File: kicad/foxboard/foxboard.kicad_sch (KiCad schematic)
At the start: 183 parts, among them J2 USB_C_Receptacle_USB2.0, K1 KEYSW, K10 KEYSW, K11 KEYSW, K12 KEYSW, K13 KEYSW, K14 KEYSW, K15 KEYSW, K16 KEYSW, K17 KEYSW, K18 KEYSW, K19 KEYSW, K2 KEYSW, K20 KEYSW, K21 KEYSW, K22 KEYSW, K23 KEYSW, K24 KEYSW, K25 KEYSW, K26 KEYSW, K27 KEYSW, K28 KEYSW, K29 KEYSW, K3 KEYSW, K30 KEYSW, K31 KEYSW, K32 KEYSW, K33 KEYSW, K34 KEYSW, K35 KEYSW, K36 KEYSW, K37 KEYSW, K38 KEYSW, K39 KEYSW, K4 KEYSW, K40 KEYSW, K41 KEYSW, K42 KEYSW, K43 KEYSW, K44 KEYSW, K45 KEYSW, K46 KEYSW, K47 KEYSW, K48 KEYSW, K49 KEYSW, K5 KEYSW, K50 KEYSW, K51 KEYSW, K52 KEYSW, K53 KEYSW, K54 KEYSW, K55 KEYSW, K56 KEYSW, K57 KEYSW, K58 KEYSW, K59 KEYSW, K6 KEYSW, K60 KEYSW, K61 KEYSW, K62 KEYSW, K63 KEYSW, K64 KEYSW, K65 KEYSW, K66 KEYSW, K67 KEYSW, K68 KEYSW, K69 KEYSW, K7 KEYSW, K70 KEYSW, K71 KEYSW, K72 KEYSW, K73 KEYSW, K74 KEYSW, K75 KEYSW, K76 KEYSW, K77 KEYSW, K78 KEYSW, K79 KEYSW, K8 KEYSW, K80 KEYSW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

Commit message: make sure all connections are connected, change resistor package to 0805
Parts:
- D52: MPN C2875153 -> C24372
- R5, R6: footprint custom:RESC1608X55N -> Resistor_SMD:R_0805_2012Metric
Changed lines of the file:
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@@
 			)
 		)
-		(property "Footprint" "custom:RESC1608X55N"
+		(property "Footprint" "Resistor_SMD:R_0805_2012Metric"
 			(at 254 160.528 90)
 			(effects
@@
 			)
 		)
-		(property "MPN" "C2875153"
+		(property "MPN" "C24372"
 			(at 45.72 86.36 90)
 			(effects
@@
 			)
 		)
-		(property "Footprint" "custom:RESC1608X55N"
+		(property "Footprint" "Resistor_SMD:R_0805_2012Metric"
 			(at 254 157.988 90)
 			(effects

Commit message: fix
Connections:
- net row 5: now also U2.5 (3_LRCLK2); no longer U2.2 (0_RX1_CRX2_CS1)
- net row 6: now also U2.6 (4_BCLK2); no longer U2.1 (GND)

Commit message: wip v2
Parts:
- removed U2: Teensy4.1, teensy:Teensy41, symbol teensy:Teensy4.1
- added C1, C2: 10u, symbol Device:C
- added C10, C11, C12, C13, C5, C6, C7, C8, C9: 100n, symbol Device:C
- added C14, C3: 1u, symbol Device:C
- added C15, C4: C, symbol Device:C
- added C16, C17: 15p, symbol Device:C
- added J1: Conn_01x02, symbol Connector_Generic:Conn_01x02
- added R1, R2: 27.4, symbol Device:R
- added R3: 1k, symbol Device:R
- added R4: DNF, symbol Device:R
- added U1: RP2040, RP2040_minimal:RP2040-QFN-56, symbol MCU_RaspberryPi_RP2040:RP2040
- added U2: NCP1117-3.3_SOT223, Package_TO_SOT_SMD:SOT-223-3_TabPin2, symbol Regulator_Linear:NCP1117-3.3_SOT223
- added U3: W25Q128JVS, Package_SO:SOIC-8_5.3x5.3mm_P1.27mm, symbol Memory_Flash:W25Q128JVS
- added Y1: ABM8-272-T3, symbol Device:Crystal_GND24
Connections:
- net GND: now also C1.2, C10.2, C11.2, C12.2, C13.2, C14.2, C15.2, C16.1, C17.1, C2.1, C3.2, C4.2, C5.2, C6.2, C7.2, C8.2, C9.2, J1.1 (Pin_1), U2.1 (GND), U3.4 (GND), Y1.2 (G), Y1.4 (G)
- net VBUS: now also C1.1, U2.3 (VI)
- net col 1: now also U1.8 (GPIO6)
- net col 10: now also U1.18 (GPIO15)
- net col 11: now also U1.27 (GPIO16)
- net col 12: now also U1.28 (GPIO17)
- net col 13: now also U1.29 (GPIO18)
- net col 14: now also U1.30 (GPIO19)
- net col 15: now also U1.31 (GPIO20)
- net col 16: now also U1.32 (GPIO21)
- net col 17: now also U1.34 (GPIO22)
- net col 2: now also U1.9 (GPIO7)
- net col 3: now also U1.11 (GPIO8)
- net col 4: now also U1.12 (GPIO9)
- net col 5: now also U1.13 (GPIO10)
- net col 6: now also U1.14 (GPIO11)
- net col 7: now also U1.15 (GPIO12)
- net col 8: now also U1.16 (GPIO13)
- net col 9: now also U1.17 (GPIO14)
- net row 1: now also U1.2 (GPIO0)
- net row 2: now also U1.3 (GPIO1)
- net row 3: now also U1.4 (GPIO2)
- net row 4: now also U1.5 (GPIO3)
- net row 5: now also U1.6 (GPIO4)
- net row 6: now also U1.7 (GPIO5)
- net USB_D-: now reaches J2.A7 (D-), J2.B7 (D-)
- net USB_D-: now also R1.2
- net USB_D+: now reaches J2.A6 (D+), J2.B6 (D+)
- net USB_D+: now also R2.1
- new net: R3.1, R4.2, U3.1 (~{CS})
- new net: J1.2 (Pin_2), R3.2
- new net: R2.2, U1.46 (USB_DM)
- new net: R1.1, U1.47 (USB_DP)
- new net +1.1V: C3.1, C4.1, C5.1, U1.23 (DVDD), U1.45 (VREG_VOUT), U1.50 (DVDD)
- new net +3.3V: C10.1, C11.1, C12.1, C13.1, C14.1, C15.1, C2.2, C6.1, C7.1, C8.1, C9.1, R4.1, U1.1 (IOVDD), U1.10 (IOVDD), U1.22 (IOVDD), U1.33 (IOVDD), U1.42 (IOVDD), U1.43 (ADC_AVDD), U1.44 (VREG_IN), U1.48 (USB_VDD), U1.49 (IOVDD), U2.2 (VO), U3.8 (VCC)
- new net XIN: C17.2, U1.20 (XIN), Y1.1
- new net XOUT: C16.2, U1.21 (XOUT), Y1.3
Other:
- moved on the sheet: J2, R5, R6

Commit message: fix most violations
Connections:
- net GND: now also U1.19 (TESTEN), U1.57 (GND)
- net QSPI_SS: now reaches R3.1, R4.2, U3.1 (~{CS})
- net QSPI_SS: now also U1.56 (QSPI_SS)
- net QSPI_SD3: now reaches U1.51 (QSPI_SD3)
- net QSPI_SD3: now also U3.7 (~{HOLD}/~{RESET}/IO_{3})
- net QSPI_SCLK: now reaches U1.52 (QSPI_SCLK)
- net QSPI_SCLK: now also U3.6 (CLK)
- net QSPI_SDO: now reaches U1.53 (QSPI_SD0)
- net QSPI_SDO: now also U3.5 (DI/IO_{0})
- net QSPI_SD2: now reaches U1.54 (QSPI_SD2)
- net QSPI_SD2: now also U3.3 (~{WP}/IO_{2})
- net QSPI_SD1: now reaches U1.55 (QSPI_SD1)
- net QSPI_SD1: now also U3.2 (DO/IO_{1})
- no-connect marks 2 -> 12
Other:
- moved on the sheet: J1, R3

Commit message: add powerflags
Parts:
- D56:  MPN C24372 -> (none); MPN (none) -> C24372
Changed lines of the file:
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@@
 	)
 	(junction
-		(at 55.88 236.22)
-		(diameter 0)
-		(color 0 0 0 0)
-	)
-	(junction
 		(at 317.5 49.53)
 		(diameter 0)
@@
 	)
 	(junction
+		(at 347.98 161.29)
+		(diameter 0)
+		(color 0 0 0 0)
+	)
+	(junction
 		(at 250.19 90.17)
 		(diameter 0)
@@
 	)
 	(junction
+		(at 55.88 236.22)
+		(diameter 0)
+		(color 0 0 0 0)
+	)
+	(junction
 		(at 238.76 124.46)
 		(diameter 0)
@@
 	)
 	(junction
+		(at 165.1 284.48)
+		(diameter 0)
+		(color 0 0 0 0)
+	)
+	(junction
 		(at 231.14 73.66)
 		(diameter 0)
@@
 	(wire
 		(pts
+			(xy 55.88 236.22) (xy 71.12 236.22)
+		)
+		(stroke
+			(width 0)
+			(type default)
+		)
+	)
+	(wire
+		(pts
 			(xy 60.96 82.55) (xy 60.96 100.33)
 		)
@@
 	(wire
 		(pts
+			(xy 165.1 284.48) (xy 172.72 284.48)
+		)
+		(stroke
+			(width 0)
+			(type default)
+		)
+	)
+	(wire
+		(pts
 			(xy 128.27 139.7) (xy 135.89 139.7)
 		)
@@
 	(wire
 		(pts
-			(xy 55.88 236.22) (xy 69.85 236.22)
-		)
-		(stroke
-			(width 0)
-			(type default)
-		)
-	)
-	(wire
-		(pts
 			(xy 165.1 39.37) (xy 165.1 49.53)
 		)
@@
 		)
 	)
-	(label ""
-		(at 55.88 236.22 0)
-		(effects
-			(font
-				(size 1.27 1.27)
-			)
-			(justify left bottom)
-		)
-	)
 	(label "QSPI_SS"
 		(at 133.35 201.93 180)
@@
 	(global_label "XIN"
 		(shape input)
-		(at 69.85 236.22 0)
+		(at 71.12 236.22 0)
 		(fields_autoplaced yes)
 		(effects
@@
 		)
 		(property "Intersheetrefs" "${INTERSHEET_REFS}"
-			(at 75.98 236.22 0)
+			(at 77.25 236.22 0)
 			(hide yes)
 			(show_name no)
@@
 	)
 	(symbol
+		(lib_id "power:PWR_FLAG")
+		(at 172.72 284.48 0)
+		(unit 1)
+		(body_style 1)
+		(exclude_from_sim no)
+		(in_bom yes)
+		(on_board yes)
+		(in_pos_files yes)
+		(dnp no)
+		(fields_autoplaced yes)
+		(property "Reference" "#FLG01"
+			(at 172.72 282.575 0)
+			(hide yes)
+			(show_name no)
+			(do_not_autoplace no)
+			(effects
+				(font
+					(size 1.27 1.27)
+				)
+			)
+		)
+		(property "Value" "PWR_FLAG"
+			(at 172.72 279.4 0)
+			(show_name no)
+			(do_not_autoplace no)
+			(effects
+				(font
+					(size 1.27 1.27)
+				)
+			)
+		)
+		(property "Footprint" ""
+			(at 172.72 284.48 0)
+			(hide yes)
+			(show_name no)
+			(do_not_autoplace no)
+			(effects
+				(font
+					(size 1.27 1.27)
+				)
+			)
+		)
+		(property "Datasheet" ""
+			(at 172.72 284.48 0)
+			(hide yes)
+			(show_name no)
+			(do_not_autoplace no)
+			(effects
+				(font
+					(size 1.27 1.27)
+				)
+			)
+		)
+		(property "Description" "Special symbol for telling ERC where power comes from"
+			(at 172.72 284.48 0)
+			(hide yes)
+			(show_name no)
+			(do_not_autoplace no)
+			(effects
+				(font
+					(size 1.27 1.27)
+				)
+			)
+		)
+		(pin "1"
+		)
+		(instances
+			(project "foxboard"
+				(path "/06390bb7-84c9-4afb-a691-da3db02fcaf4"
+					(reference "#FLG01")
+					(unit 1)
+				)
+			)
+		)
+	)
+	(symbol
 		(lib_id "Device:D")
 		(at 26.67 120.65 90)
@@
 		(in_pos_files yes)
 		(dnp no)
-		(fields_autoplaced yes)
 		(property "Reference" "#PWR06"
 			(at 345.44 163.83 0)
@@
 		)
 		(property "Value" "VBUS"
-			(at 345.44 154.94 0)
+			(at 345.44 155.702 0)
 			(show_name no)
 			(do_not_autoplace no)
@@
 			)
 		)
-		(property " MPN" "C24372"
+		(property "MPN" "C24372"
 			(at 129.54 86.36 90)
 			(hide yes)
@@
 					(unit 1)
 				)
+			)
+		)
+	)
+	(symbol
+		(lib_id "power:PWR_FLAG")
+		(at 347.98 161.29 0)
+		(unit 1)
+		(body_style 1)
+		(exclude_from_sim no)
+		(in_bom yes)
+		(on_board yes)
+		(in_pos_files yes)
+		(dnp no)
+		(fields_autoplaced yes)
+		(property "Reference" "#FLG02"
+			(at 347.98 159.385 0)
+			(hide yes)
+			(show_name no)
+			(do_not_autoplace no)
+			(effects
+				(font
+					(size 1.27 1.27)
+				)
+			)
+		)
+		(property "Value" "PWR_FLAG"
+			(at 347.98 156.21 0)
+			(show_name no)
+			(do_not_autoplace no)
+			(effects
+				(font
+					(size 1.27 1.27)
+				)
+			)
+		)
+		(property "Footprint" ""
+			(at 347.98 161.29 0)
+			(hide yes)
+			(show_name no)
+			(do_not_autoplace no)
+			(effects
+				(font
+					(size 1.27 1.27)
+				)
+			)
+		)
+		(property "Datasheet" ""
+			(at 347.98 161.29 0)
+			(hide yes)
+			(show_name no)
+			(do_not_autoplace no)
+			(effects
+				(font
+					(size 1.27 1.27)
+				)
+			)
+		)
+		(property "Description" "Special symbol for telling ERC where power comes from"
+			(at 347.98 161.29 0)
+			(hide yes)
+			(show_name no)
+			(do_not_autoplace no)
+			(effects
+				(font
+					(size 1.27 1.27)
+				)
+			)
+		)
+		(pin "1"
+		)
+		(instances
+			(project "foxboard"
+				(path "/06390bb7-84c9-4afb-a691-da3db02fcaf4"
+					(reference "#FLG02")
+					(unit 1)
+				)

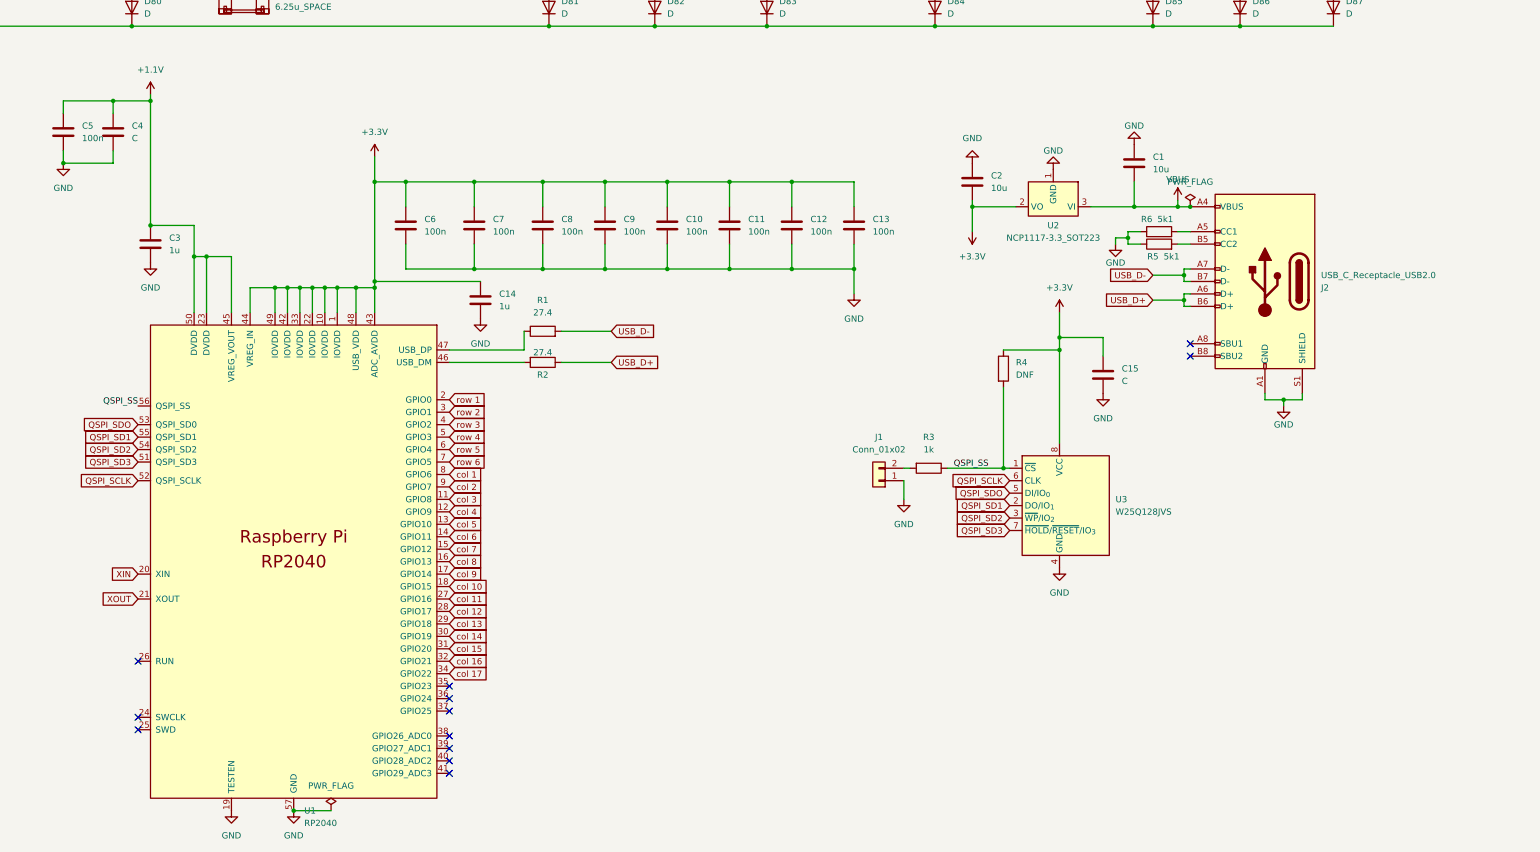
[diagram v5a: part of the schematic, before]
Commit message: fix all warnings
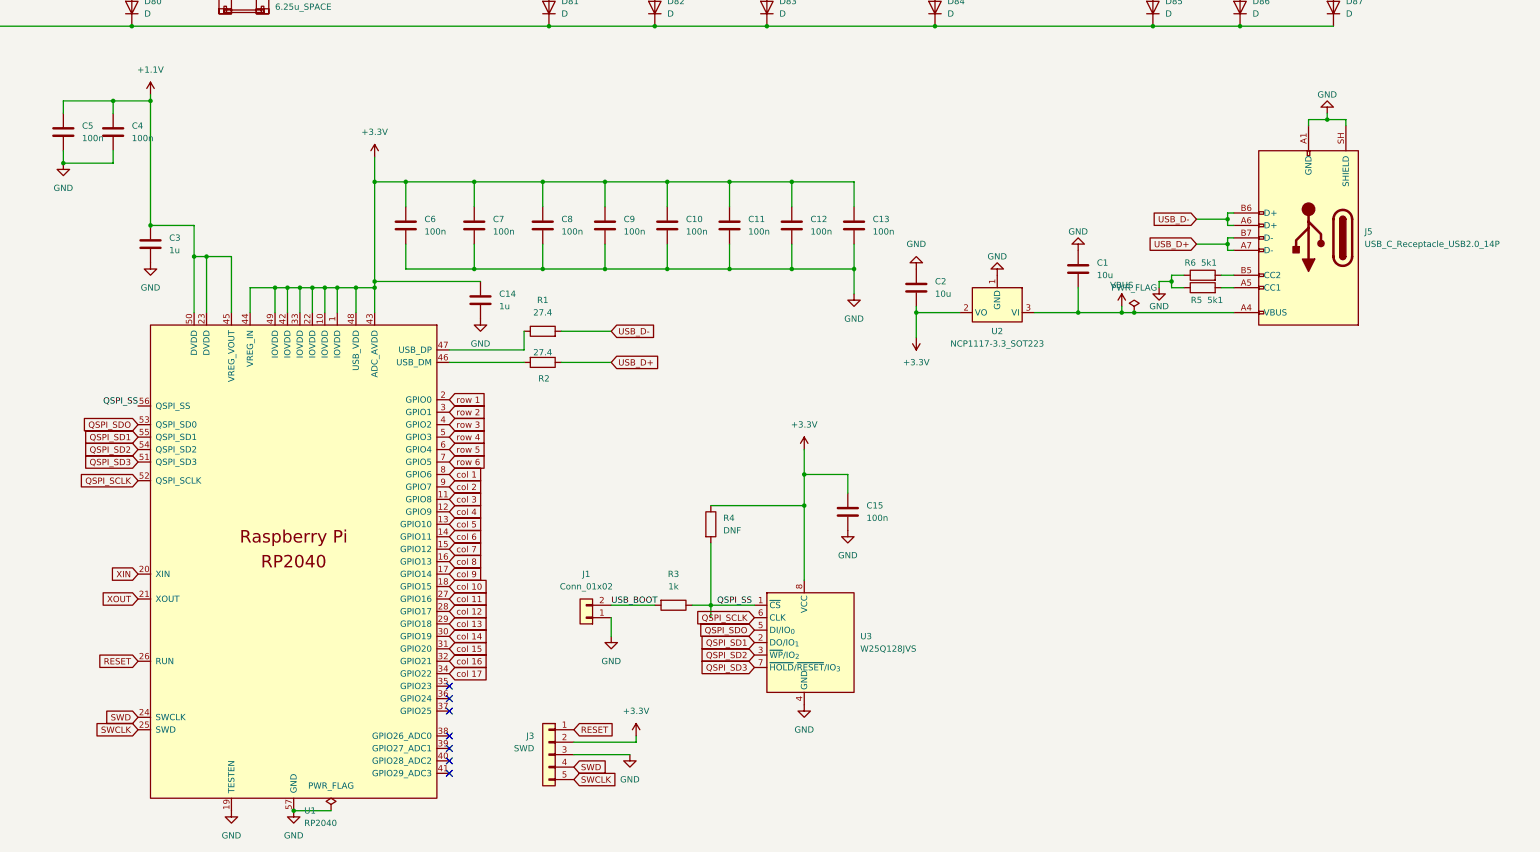
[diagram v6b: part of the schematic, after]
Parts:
- removed J2: USB_C_Receptacle_USB2.0, Connector_USB:USB_C_Receptacle_HRO_TYPE-C-31-M-12, symbol Connector:USB_C_Receptacle_USB2.0
- added J3: SWD, Connector_PinSocket_2.54mm:PinSocket_1x05_P2.54mm_Vertical, symbol Connector_Generic:Conn_01x05
- added J5: USB_C_Receptacle_USB2.0_14P, symbol Connector:USB_C_Receptacle_USB2.0_14P
- C1, C10, C11, C12, C13, C14, C16, C2, C3, C5, C6, C7, C8, C9: footprint (none) -> Capacitor_SMD:C_0402_1005Metric_Pad0.74x0.62mm_HandSolder
- C15, C4: value C -> 100n; footprint (none) -> Capacitor_SMD:C_0402_1005Metric_Pad0.74x0.62mm_HandSolder
- C17: footprint (none) -> Capacitor_SMD:C_0402_1005Metric
- D1, D10, D11, D12, D13, D14, D15, D16, D17, D18, D19, D2, D20, D21, D22, D23, D24, D25, D26, D27, D28, D29, D3, D30, D31, D32, D33, D34, D35, D36, D37, D38, D39, D4, D40, D41, D42, D43, D44, D45, D46, D47, D48, D49, D5, D50, D51, D52, D53, D54, D55, D56, D57, D58, D59, D6, D60, D61, D62, D63, D64, D65, D66, D67, D68, D69, D7, D70, D71, D72, D73, D74, D75, D76, D77, D78, D79, D8, D80, D81, D82, D83, D84, D85, D86, D87, D9: footprint Diode_SMD:D_SOD-323 -> 1N4148:DIOAD753W49L380D172B
- U1: footprint RP2040_minimal:RP2040-QFN-56 -> custom:RP2040-QFN-56
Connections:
- net +3.3V: now also J3.2 (Pin_2)
- net GND: now also J3.3 (Pin_3), J5.A1 (GND), J5.A12 (GND), J5.B1 (GND), J5.B12 (GND), J5.SH (SHIELD)
- net USB_D+: now also J5.A7 (D-), J5.B7 (D-)
- net USB_D-: now also J5.A6 (D+), J5.B6 (D+)
- net VBUS: now also J5.A4 (VBUS), J5.A9 (VBUS), J5.B4 (VBUS), J5.B9 (VBUS)
- net USB_BOOT: now reaches J1.2 (Pin_2), R3.2
- net at R6.2: now also J5.B5 (CC2)
- net at R5.2: now also J5.A5 (CC1)
- net SWD: now reaches U1.24 (SWCLK)
- net SWD: now also J3.4 (Pin_4)
- net SWCLK: now reaches U1.25 (SWD)
- net SWCLK: now also J3.5 (Pin_5)
- net RESET: now reaches U1.26 (RUN)
- net RESET: now also J3.1 (Pin_1)
- no-connect marks 12 -> 7
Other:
- moved on the sheet: C1, C15, C2, J1, R3, R4, R5, R6, U2, U3

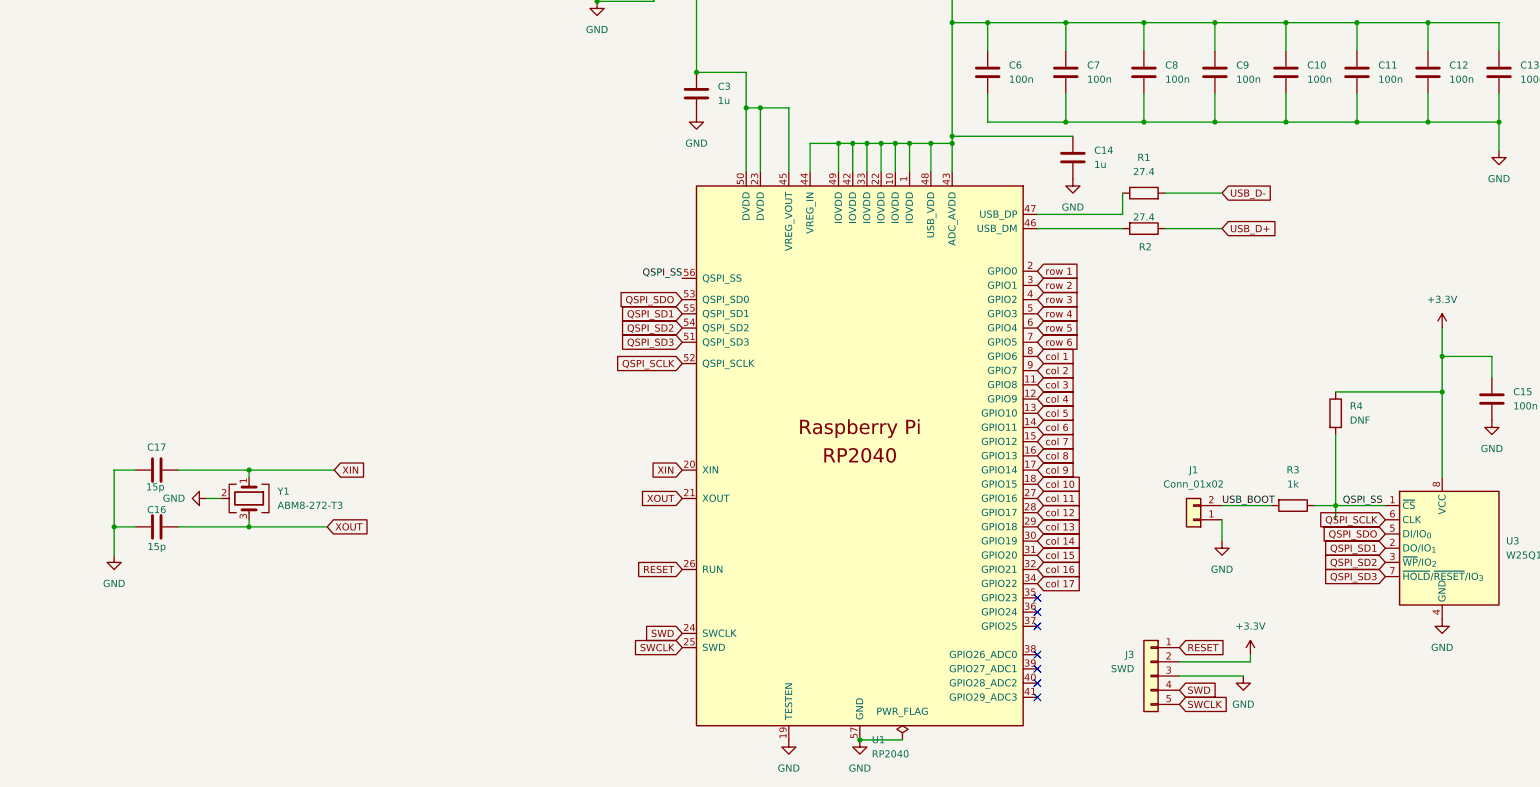
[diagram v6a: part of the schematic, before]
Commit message: assigned footprints
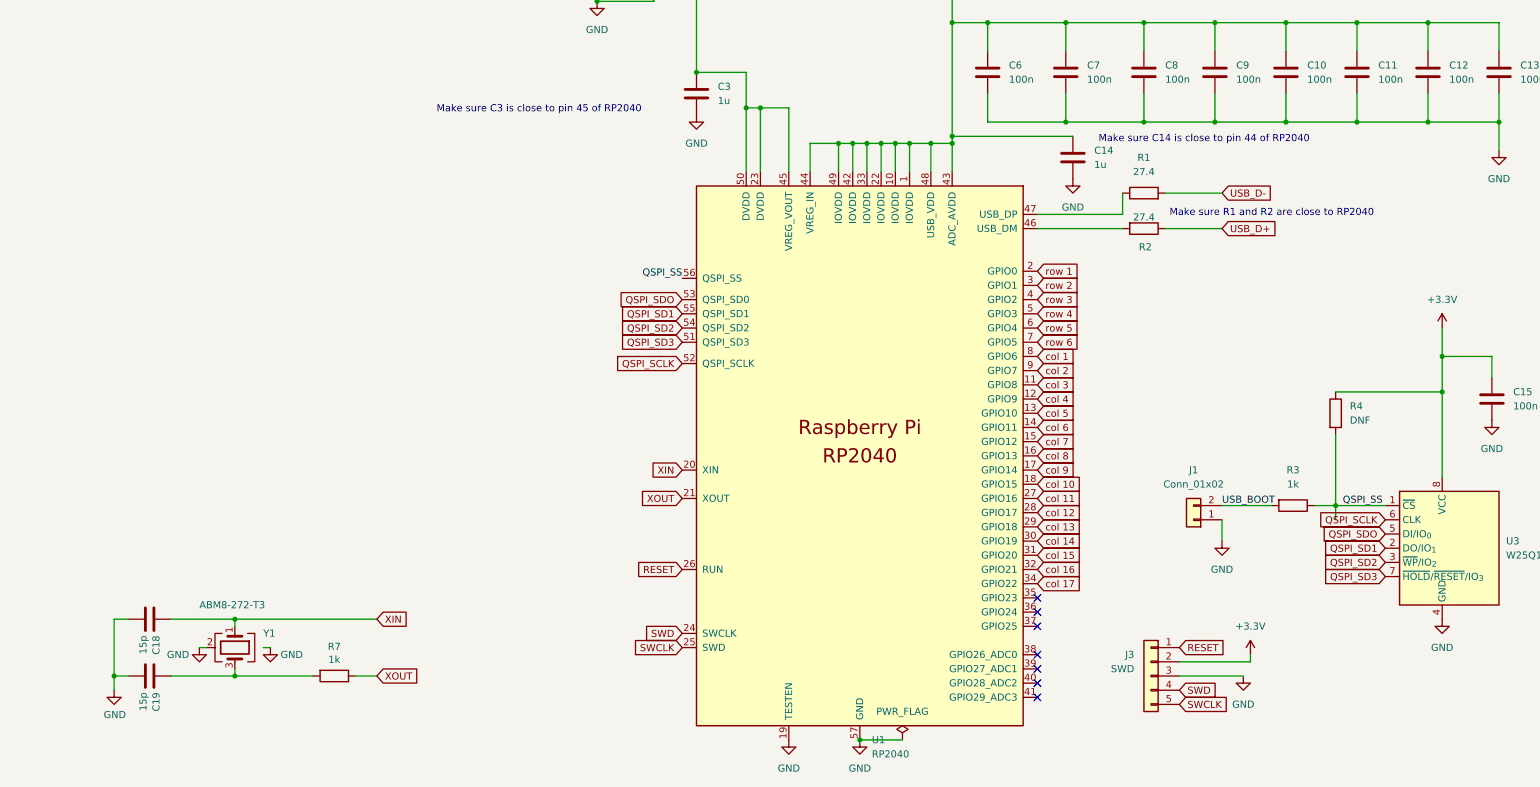
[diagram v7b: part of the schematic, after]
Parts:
- removed C16: 15p, Capacitor_SMD:C_0402_1005Metric_Pad0.74x0.62mm_HandSolder, symbol Device:C
- removed C17: 15p, Capacitor_SMD:C_0402_1005Metric, symbol Device:C
- added C18, C19: 15p, Capacitor_SMD:C_0402_1005Metric, symbol Device:C
- added R7: 1k, Resistor_SMD:R_0402_1005Metric_Pad0.72x0.64mm_HandSolder, symbol Device:R
- J1: footprint (none) -> Connector_PinHeader_2.54mm:PinHeader_1x02_P2.54mm_Vertical
- J5: footprint (none) -> Connector_USB:USB_C_Receptacle_HRO_TYPE-C-31-M-12
- R1, R2, R3, R4: footprint (none) -> Resistor_SMD:R_0402_1005Metric_Pad0.72x0.64mm_HandSolder
- R5, R6: footprint Resistor_SMD:R_0805_2012Metric -> Resistor_SMD:R_0402_1005Metric_Pad0.72x0.64mm_HandSolder
- Y1: footprint (none) -> Crystal:Crystal_SMD_3225-4Pin_3.2x2.5mm; private KLC_S4.1 -> (none)
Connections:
- net GND: now also C18.2, C19.2
- net XIN: now also C18.1
- net XOUT: now also R7.1; no longer Y1.3
- new net: C19.1, R7.2, Y1.3
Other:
- note added: "Make sure C14 is close to pin 44 of RP2040"
- note added: "Make sure C3 is close to pin 45 of RP2040"
- note added: "Make sure R1 and R2 are close to RP2040"
